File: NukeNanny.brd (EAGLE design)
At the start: 35 x 21.5 mm, 46 parts, among them IC1 25AA080SN, Q1 MMBT4403, U1 CR2032, U2 SHT1XSMD, U3 HX711

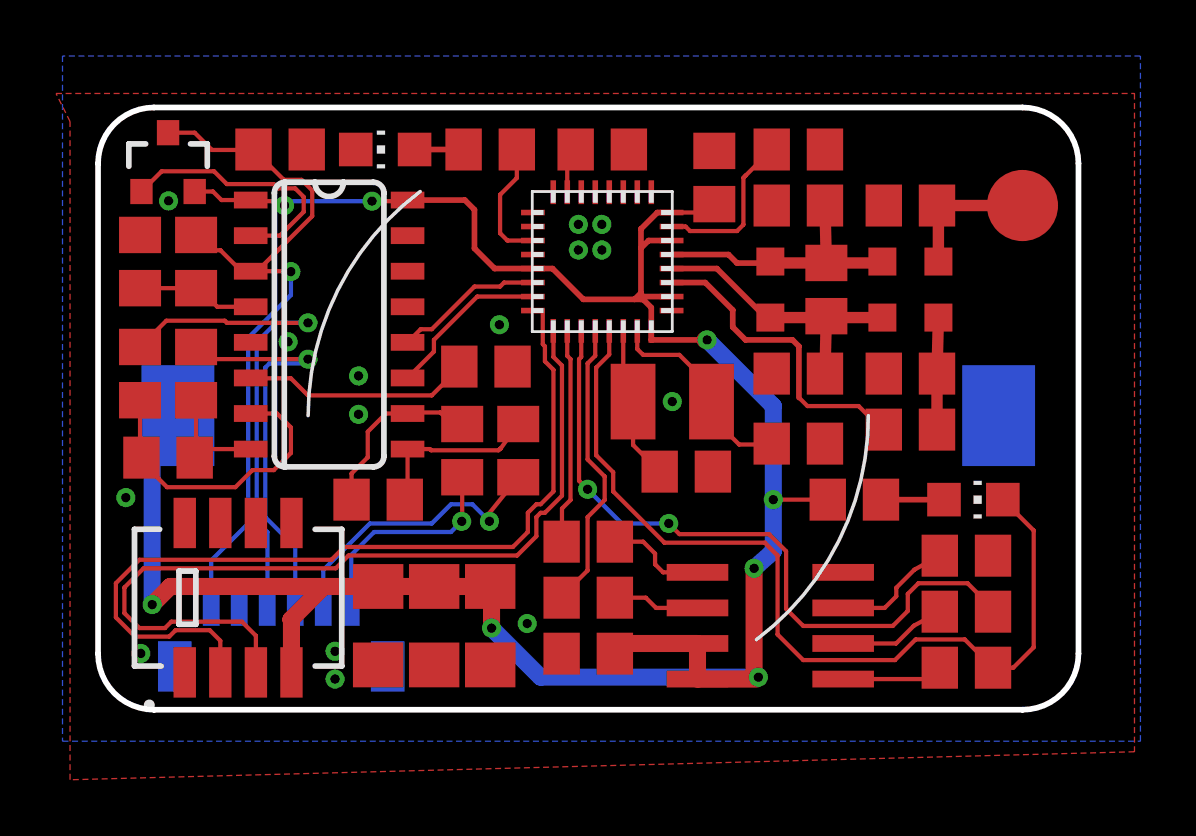
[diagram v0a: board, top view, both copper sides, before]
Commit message: Changed sensor to HTU21D
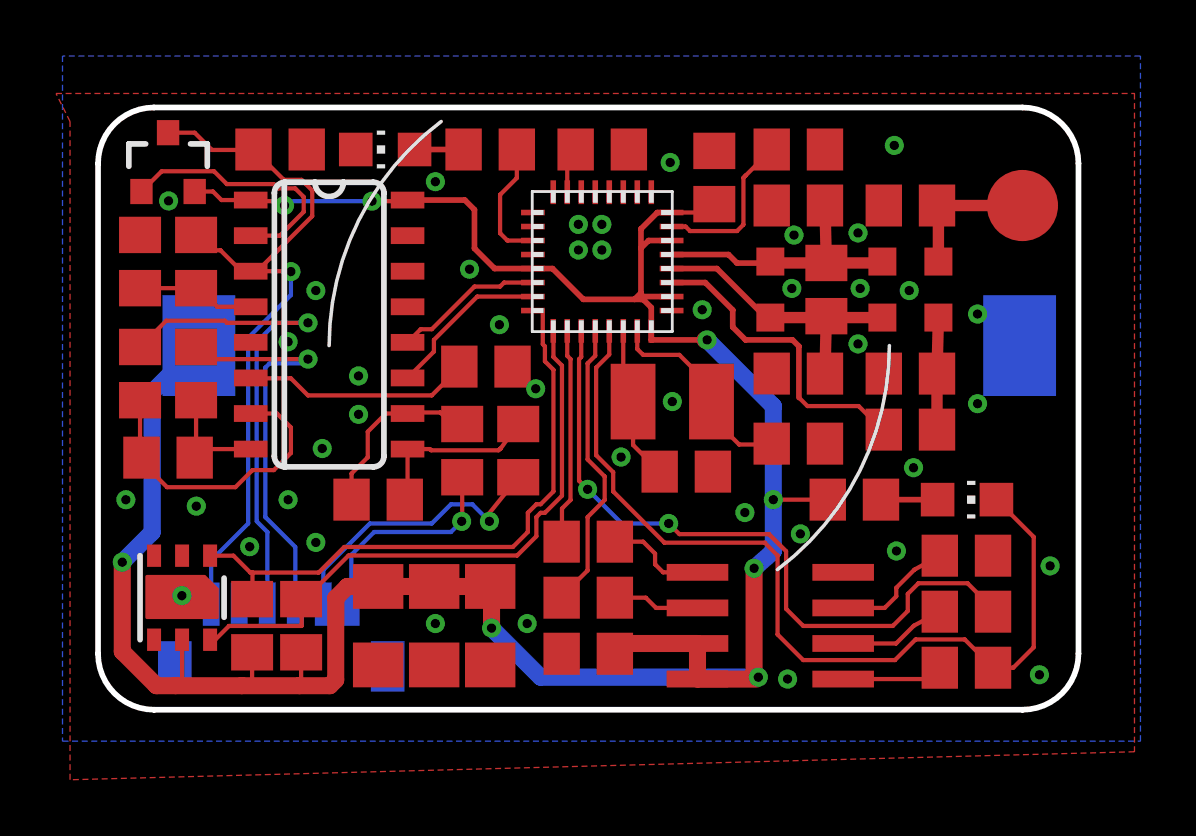
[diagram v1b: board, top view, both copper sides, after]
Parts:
- removed U2: SHT1XSMD, SparkFun-Sensors:SHT1X
- added R13, R16: 1k, rcl:R0805
- added U4: HTU21D, SparkFun-Sensors:HTU21D
- C11: value 6.8p -> 0.1u
- C9: value 3.3 -> 3.3p
- R1, R2: value (none) -> 200
- moved U1 2.61 mm to (80.2, 19.0)
- moved LED1 0.23 mm to (93.0, 13.5)
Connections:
- net GND: now also U4.7, U4.GND; no longer U2.1
- net SHDAT: now also R13.2, U4.DATA; no longer U2.2
- net SHSCK: now also R16.2, U4.SCK; no longer U2.3
- net VCC: now also R13.1, R16.1, U4.VDD; no longer U2.4
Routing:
- net VCC: track 86.8 -> 97.3 mm
- net SHSCK: track 30.8 -> 21.7 mm
- net SHDAT: track 31.0 -> 22.0 mm
